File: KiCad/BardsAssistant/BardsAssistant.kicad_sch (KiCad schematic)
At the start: 70 parts, among them IC1 ESP32-S3-MINI-1-N8, J1 USB_C_Receptacle_USB2.0_16P, J2 Conn_01x24, J3 JST-PH-2-SMT-RA, Q1 Si1308EDL, Q3 AO3401A, SW1 SW_Push, SW2 SW_Push, SW3 SW_Push, SW4 SW_Push, SW5 SW_Push, SW6 SW_Push, U1 TPS63001, U2 USBLC6-2SC6, U3 MCP73831/2

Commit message: Added new KiCad revision
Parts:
- added R17, R4: 1R, Resistor_SMD:R_0603_1608Metric, symbol Device:R_Small_US
- added TP7, TP8, TP9: TestPoint, TestPoint:TestPoint_Pad_2.0x2.0mm, symbol Connector:TestPoint
- C1, C5, C6: LCSC (none) -> C19702; MPN (none) -> CL10A106KP8NNNC; Manufacturer (none) -> Samsung; Notes (none) -> X5R 10V; Status (none) -> Locked
- C10, C9: LCSC (none) -> C1779; MPN (none) -> CL21A475KAQNNNE; Manufacturer (none) -> Samsung; Status (none) -> Locked
- C11, C12, C15, C16, C17, C18, C19, C20: LCSC (none) -> C15849; MPN (none) -> CL10A105KA8NNNC; Manufacturer (none) -> Samsung; Status (none) -> Locked
- C13, C7, C8: LCSC (none) -> C15849; MPN (none) -> CL10A105KB8NNNC; Manufacturer (none) -> Samsung; Status (none) -> Locked
- C2: LCSC (none) -> C14663; MPN (none) -> CC0603KRX7R9BB104; Manufacturer (none) -> YAGEO; Notes (none) -> X5R 50V bc 10V is extended parts catalog in jlc.; Status (none) -> Locked
- C21, C22: LCSC (none) -> C19702; MPN (none) -> CL10A106KP8NNNC; Manufacturer (none) -> Samsung; Status (none) -> Locked
- C3: LCSC (none) -> C45783; MPN (none) -> CL21A226MAQNNNE; Manufacturer (none) -> Samsung; Notes (none) -> 25V; Status (none) -> Locked
- C4: footprint Capacitor_SMD:C_0805_2012Metric -> Capacitor_SMD:C_0603_1608Metric; LCSC (none) -> C14663; MPN (none) -> CC0603KRX7R9BB104; Manufacturer (none) -> Yaego; Notes (none) -> Using 50V bc 10v is extended parts catalog for jlc; Status (none) -> Locked
- D1: LCSC (none) -> C965844; MPN (none) -> XL-3227RGB-RF; Manufacturer (none) -> XINGLIGHT; Status (none) -> Locked
- D2: LCSC (none) -> C2480; MPN (none) -> SS14; Manufacturer (none) -> MDD(Microdiode Semiconductor); Status (none) -> Locked
- D3, D4: LCSC (none) -> C96512; MPN (none) -> ESD9B3.3ST5G; Manufacturer (none) -> onsemi; Status (none) -> Locked
- D5: LCSC (none) -> C2286; MPN (none) -> KT-0603R; Manufacturer (none) -> Hubei KENTO Elec; Status (none) -> Locked
- D6, D7, D8: LCSC (none) -> C77336; MPN (none) -> MBR0530; Manufacturer (none) -> Jiangsu Changjing Electronics Technology Co., Ltd.; Status (none) -> Locked
- D9: footprint LED_SMD:LED_0603_1608Metric -> LED_SMD:LED_0805_2012Metric; LCSC (none) -> C2297; MPN (none) -> KT-0805G; Manufacturer (none) -> Hubei KENTO Elec; Status (none) -> Locked
- F1: footprint Fuse:Fuse_1206_3216Metric -> Fuse:Fuse_0805_2012Metric; LCSC (none) -> C5307781; MPN (none) -> JK-SMD0805-100-6; Manufacturer (none) -> Jinrui Electronic Materials Co.; Status (none) -> Locked
- FB1: LCSC (none) -> C85840; MPN (none) -> BLM21PG221SN1D; Manufacturer (none) -> Murata Electronics; Status (none) -> Locked
- IC1: footprint ESP32S3MINI1N8 -> ESP32-S3-MINI-1-N8:ESP32S3MINI1N8; Height 2.55 -> (none); LCSC (none) -> C2913206; MPN (none) -> ESP32-S3-MINI-1-N8; Manufacturer (none) -> Espressif Systems; Mouser Part Number 356-ESP32-S3-MINI1N8 -> (none); Mouser Price/Stock https://www.mouser.co.uk/ProductDetail/Espressif-Systems/ES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 -> (none); Status (none) -> Locked
- J1: LCSC (none) -> C5143397; MPN (none) -> USB4110-GF-A; Manufacturer (none) -> GCT; Status (none) -> Locked
- J2: footprint Connector_FFC-FPC:Hirose_FH12-24S-0.5SH_1x24-1MP_P0.50mm_Horizontal -> BardAssLibrary:FPC-SMD_KH-FG0.5-H2.0-24PIN; LCSC (none) -> C2797213; MPN (none) -> KH-FG0.5-H2.0-24PIN; Manufacturer (none) -> Shenzhen Kinghelm Elec; Notes (none) -> Verify against data sheet
- J3: LCSC (none) -> C157932; MPN (none) -> S2B-PH-K-S-GW; Manufacturer (none) -> JST; Status (none) -> Locked
- L1: LCSC (none) -> C53663; MPN (none) -> SWPA6045S680MT; Manufacturer (none) -> Sunlord; Status (none) -> Locked
- L2: footprint Inductor_SMD:L_Wuerth_MAPI-4020 -> BardAssLibrary:SMNR5040_2R2MT_BA; LCSC (none) -> C9941; MPN (none) -> SMNR5040-2R2MT; Manufacturer (none) -> Shenzhen Shun Xiang Nuo Electronics; Status (none) -> Locked
- Q1: LCSC (none) -> C469327; MPN (none) -> SI1308EDL-T1-GE3; Manufacturer (none) -> Vishay; Status (none) -> Locked
- Q3: LCSC (none) -> C15127; MPN (none) -> AO3401A; Manufacturer (none) -> Alpha & Omega Semicon; Status (none) -> Locked
- R1, R10, R2: LCSC (none) -> C25905; MPN (none) -> 0402WGF5101TCE; Manufacturer (none) -> Uni-Royal; Status (none) -> Locked
- R11, R14, R16: LCSC (none) -> C23138; MPN (none) -> 0603WAF3300T5E; Manufacturer (none) -> Uni-Royal; Status (none) -> Locked
- R12, R13: LCSC (none) -> C25117; MPN (none) -> 0402WGF4700TCE; Manufacturer (none) -> Uni-Royal; Status (none) -> Locked
- R15: LCSC (none) -> C25076; MPN (none) -> 0402WGF1000TCE; Manufacturer (none) -> Uni-Royal; Status (none) -> Locked
- R3, R5, R7, R8: LCSC (none) -> C25744; MPN (none) -> 0402WGF1002TCE; Manufacturer (none) -> Uni-Royal; Status (none) -> Locked
- R6: LCSC (none) -> C25741; MPN (none) -> 0402WGF1003TCE; Manufacturer (none) -> Uni-Royal; Status (none) -> Locked
- R9: value 3R -> 1R; footprint Resistor_SMD:R_0402_1005Metric -> Resistor_SMD:R_0603_1608Metric; LCSC (none) -> C22936; MPN (none) -> 0603WAF100KT5E; Manufacturer (none) -> Uni-Royal; Status (none) -> Locked
- SW1, SW2, SW3, SW4, SW5, SW6: footprint Button_Switch_SMD:SW_Push_1P1T_XKB_TS-1187A -> Button_Switch_SMD:SW_SPST_TS-1088-xR020; LCSC (none) -> C720477; MPN (none) -> TS-1088-AR02016; Manufacturer (none) -> XUNPU; Status (none) -> Locked
- U1: LCSC (none) -> C28060; MPN (none) -> TPS63001DRCR; Manufacturer (none) -> Texas Instruments; Notes (none) -> Check footprint; Status (none) -> Locked
- U2: LCSC (none) -> C7519; MPN (none) -> USBLC6-2SC6; Manufacturer (none) -> STMicroelectronics; Status (none) -> Locked
- U3: LCSC (none) -> C424093; MPN (none) -> MCP73831T-2ACI/OT; Manufacturer (none) -> Microchip Tech; Notes (none) -> Exact Adafuit chip used; Status (none) -> Locked
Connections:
- net GND: now also R17.2; no longer R9.2
- net at IC1.25 (IO21): now also TP7.1
- net TP8: now reaches IC1.5 (IO1)
- net TP8: now also TP8.1
- net TP9: now reaches IC1.6 (IO2)
- net TP9: now also TP9.1
- new net: R4.1, R9.2
- new net: R17.1, R4.2
- no-connect marks 39 -> 36
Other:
- note added: "R4,R9,R17 Originally 3R, but extended parts so 1R x 3 in series should be close enough"
- note removed: "HRO TYPE-C-31-M-12"
- moved on the sheet: R9

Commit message: updated pcb v1
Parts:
- removed TP6: TestPoint, TestPoint:TestPoint_Pad_2.0x2.0mm, symbol Connector:TestPoint
- C1, C21, C22, C5, C6: LCSC C19702 -> (none); LCSC Part # (none) -> C19702
- C10, C9: LCSC C1779 -> (none); LCSC Part # (none) -> C1779
- C11, C12, C15, C16, C17, C18, C19, C20: LCSC C15849 -> (none); LCSC Part # (none) -> C1712; MPN CL10A105KA8NNNC -> CL21B105KAFNFNE
- C13, C7, C8: LCSC C15849 -> (none); LCSC Part # (none) -> C1712; MPN CL10A105KB8NNNC -> CL21B105KAFNFNE
- C2: LCSC C14663 -> (none); LCSC Part # (none) -> C14663; Notes X5R 50V bc 10V is extended parts catalog in jlc. -> (none)
- C3: LCSC C45783 -> (none); LCSC Part # (none) -> C45783
- C4: LCSC C14663 -> (none); LCSC Part # (none) -> C14663; Notes Using 50V bc 10v is extended parts catalog for jlc -> (none)
- D1: LCSC C965844 -> (none); LCSC Part # (none) -> C965844
- D2: LCSC C2480 -> (none); LCSC Part # (none) -> C2480
- D3, D4: LCSC C96512 -> (none); LCSC Part # (none) -> C96512
- D5: LCSC C2286 -> (none); LCSC Part # (none) -> C2286
- D6, D7, D8: LCSC C77336 -> (none); LCSC Part # (none) -> C77336
- D9: LCSC C2297 -> (none); LCSC Part # (none) -> C2297
- F1: LCSC C5307781 -> (none); LCSC Part # (none) -> C5307781
- FB1: LCSC C85840 -> (none); LCSC Part # (none) -> C85840
- IC1: LCSC C2913206 -> (none); LCSC Part # (none) -> C2913206
- J1: LCSC C5143397 -> (none); LCSC Part # (none) -> C5143397
- J2: LCSC C2797213 -> (none); LCSC Part # (none) -> C2797213; Notes Verify against data sheet -> (none); Status (none) -> Locked
- J3: LCSC C157932 -> (none); LCSC Part # (none) -> C157932
- L1: LCSC C53663 -> (none); LCSC Part # (none) -> C53663
- L2: LCSC C9941 -> (none); LCSC Part # (none) -> C9941
- Q1: LCSC C469327 -> (none); LCSC Part # (none) -> C469327
- Q3: LCSC C15127 -> (none); LCSC Part # (none) -> C15127
- R1, R10, R2: LCSC C25905 -> (none); LCSC Part # (none) -> C25905
- R11, R14, R16: LCSC C23138 -> (none); LCSC Part # (none) -> C23138
- R12, R13: LCSC C25117 -> (none); LCSC Part # (none) -> C25117
- R15: LCSC C25076 -> (none); LCSC Part # (none) -> C25076
- R17, R4, R9: LCSC C22936 -> (none); LCSC Part # (none) -> C22936
- R3, R5, R7, R8: LCSC C25744 -> (none); LCSC Part # (none) -> C25744
- R6: LCSC C25741 -> (none); LCSC Part # (none) -> C25741
- SW1, SW2, SW3, SW4, SW5, SW6: LCSC C720477 -> (none); LCSC Part # (none) -> C720477
- TP1: Notes TP1 Expected 5V -> (none); Status (none) -> Locked; now left out of the parts list
- TP2: Notes Empty ~3.2v, nominal ~3.7, full ~4.2 -> (none); Status (none) -> Locked; now left out of the parts list
- TP3: Notes plugged SYS ≈ 4.7-5V, unplugged SYS ≈ BAT -> (none); Status (none) -> Locked; now left out of the parts list
- TP4, TP7, TP8, TP9: Status (none) -> Locked; now left out of the parts list
- TP5: value TestPoint -> GND; Notes Ground -> (none); Status (none) -> Locked; now left out of the parts list
- U1: LCSC C28060 -> (none); LCSC Part # (none) -> C28060; Notes Check footprint -> (none)
- U2: LCSC C7519 -> (none); LCSC Part # (none) -> C7519
- U3: LCSC C424093 -> (none); LCSC Part # (none) -> C424093
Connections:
- net +3.3V is gone; now on net +3V3: D1.4 (A)
- net VDD33 is gone; now on net +3V3: C10.2, L1.1
- net at IC1.33 (IO37): now also TP8.1
- net at IC1.34 (IO38): now also TP9.1
- net TP8: no longer names the net of IC1.5 (IO1)
- net TP8: no longer TP8.1
- net TP9: no longer names the net of IC1.6 (IO2)
- net TP9: no longer TP9.1
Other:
- note removed: "MINI-1 Data sheet"
- moved on the sheet: TP7

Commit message: Update KiCad schematic, PCB, and library files
- Update schematic and PCB layout
- Add LED-SMD-SM1210RGB footprint to BardAssLibrary
- Remove old Gerber exports and production files, update with new
- Remove BAV1.zip
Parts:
- removed D1: XL-3227RGB-RF, BardAssLibrary:LED_XL-3227RGB-RF, symbol Device:LED_RGBA
- added D1: SM1210RGB, BardAssLibrary:LED_XL-3227RGB-RF, symbol BARDSASS:LED_RGBA_SM1210RGB_BIVAR
- added R18, R19: 22R, Resistor_SMD:R_0805_2012Metric, symbol Device:R_Small_US
- C1, C5, C6: footprint Capacitor_SMD:C_0603_1608Metric -> Capacitor_SMD:C_0805_2012Metric; LCSC Part # C19702 -> (none); MPN CL10A106KP8NNNC -> CL21B106KOYNNWE; Mouser Part Number (none) -> 187-CL21B106KOYNNWE; Notes X5R 10V -> (none)
- C10, C9: LCSC Part # C1779 -> (none); MPN CL21A475KAQNNNE -> CC0805KKX7R8BB475; Manufacturer Samsung -> Yageo; Mouser Part Number (none) -> 603-CC805KKX7R8BB475
- C11, C12, C15, C16, C17, C18, C19, C20: LCSC Part # C1712 -> (none); MPN CL21B105KAFNFNE -> CC0805KFX7R8BB105; Manufacturer Samsung -> Yageo; Mouser Part Number (none) -> 603-CC805KFX7R8BB105
- C13, C7, C8: footprint Capacitor_SMD:C_0603_1608Metric -> Capacitor_SMD:C_0805_2012Metric; LCSC Part # C1712 -> (none); MPN CL21B105KAFNFNE -> CC0805KFX7R8BB105; Manufacturer Samsung -> Yageo; Mouser Part Number (none) -> 603-CC805KFX7R8BB105
- C2: footprint Capacitor_SMD:C_0603_1608Metric -> Capacitor_SMD:C_0805_2012Metric; LCSC Part # C14663 -> (none); MPN CC0603KRX7R9BB104 -> CC0805KRX7R8BB104; Manufacturer YAGEO -> Yageo; Mouser Part Number (none) -> 603-CC805KRX7R8BB104
- C21, C22: LCSC Part # C19702 -> (none); MPN CL10A106KP8NNNC -> CL21B106KOYNNWE; Mouser Part Number (none) -> 187-CL21B106KOYNNWE
- C3: LCSC Part # C45783 -> (none); MPN CL21A226MAQNNNE -> CC0805MFX5R8BB226; Manufacturer Samsung -> Yageo; Mouser Part Number (none) -> 603-CC0805MFX5R8BB22
- C4: footprint Capacitor_SMD:C_0603_1608Metric -> Capacitor_SMD:C_0805_2012Metric; LCSC Part # C14663 -> (none); MPN CC0603KRX7R9BB104 -> CC0805KRX7R8BB104; Manufacturer Yaego -> Yageo; Mouser Part Number (none) -> 603-CC805KRX7R8BB104
- D3, D4: LCSC Part # C96512 -> (none); Mouser Part Number (none) -> 863-ESD9B3.3ST5G
- D5: footprint LED_SMD:LED_0603_1608Metric -> LED_SMD:LED_0805_2012Metric; MPN KT-0603R -> 150080SS75000; Manufacturer Hubei KENTO Elec -> Wurth Elektronik; Mouser Part Number (none) -> 710-150080SS75000
- IC1: Mouser Part Number (none) -> 356-ESP32-S3-MINI1N8
- R1, R2: footprint Resistor_SMD:R_0402_1005Metric -> Resistor_SMD:R_0805_2012Metric; LCSC Part # C25905 -> C27834; MPN 0402WGF5101TCE -> 0805W8F5101T5E
- R10: value 5K -> 5K1; footprint Resistor_SMD:R_0402_1005Metric -> Resistor_SMD:R_0805_2012Metric; LCSC Part # C25905 -> C27834; MPN 0402WGF5101TCE -> 0805W8F5101T5E
- R11, R14, R16: footprint Resistor_SMD:R_0402_1005Metric -> Resistor_SMD:R_0805_2012Metric; LCSC Part # C23138 -> C17630; MPN 0603WAF3300T5E -> 0805W8F3300T5E
- R12, R13: footprint Resistor_SMD:R_0402_1005Metric -> Resistor_SMD:R_0805_2012Metric; LCSC Part # C25117 -> C17710; MPN 0402WGF4700TCE -> 0805W8F4700T5E
- R15: footprint Resistor_SMD:R_0402_1005Metric -> Resistor_SMD:R_0805_2012Metric; LCSC Part # C25076 -> C17408; MPN 0402WGF1000TCE -> 0805W8F1000T5E
- R17, R4, R9: footprint Resistor_SMD:R_0603_1608Metric -> Resistor_SMD:R_0805_2012Metric; LCSC Part # C22936 -> C25271; MPN 0603WAF100KT5E -> 0805W8F100KT5E
- R3, R5, R7, R8: footprint Resistor_SMD:R_0402_1005Metric -> Resistor_SMD:R_0805_2012Metric; LCSC Part # C25744 -> C17414; MPN 0402WGF1002TCE -> 0805W8F1002T5E
- R6: footprint Resistor_SMD:R_0402_1005Metric -> Resistor_SMD:R_0805_2012Metric; LCSC Part # C25741 -> C149504; MPN 0402WGF1003TCE -> 0805W8F1003T5E
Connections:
- net +3V3: now also D1.1 (A)
- net D+: now also R19.1; no longer J1.A6 (D+), J1.B6 (D+)
- net D-: now also R18.1; no longer J1.A7 (D-), J1.B7 (D-)
- net at IC1.21 (IO17): now also R14.2; no longer R11.2
- net at IC1.22 (IO18): now also R11.2; no longer R14.2
- net at R16.1: now also D1.4 (BK)
- net at R14.1: now also D1.3 (GK)
- net at R11.1: now also D1.2 (RK)
- new net: J1.A6 (D+), J1.B6 (D+), R19.2
- new net: J1.A7 (D-), J1.B7 (D-), R18.2
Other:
- note added: "0805 Components and smaller board size than V1.0. Same board size as 1.1, but mouser part numbers instead. 1.1 has smaller part sizes for jlcpcb assembly."
- title: Bards Assistant V1 -> Bards Assistant V1.2

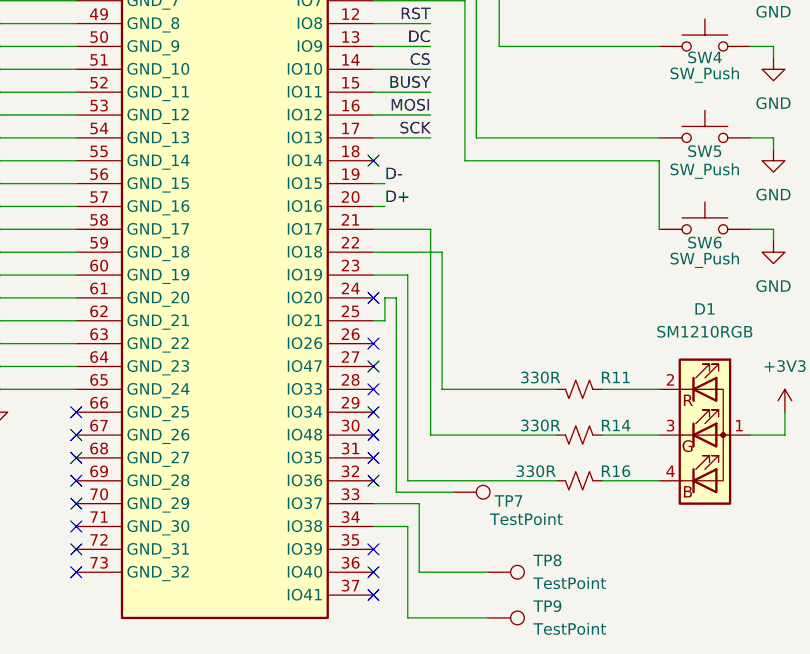
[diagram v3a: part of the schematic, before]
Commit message: update d-, d+ connection
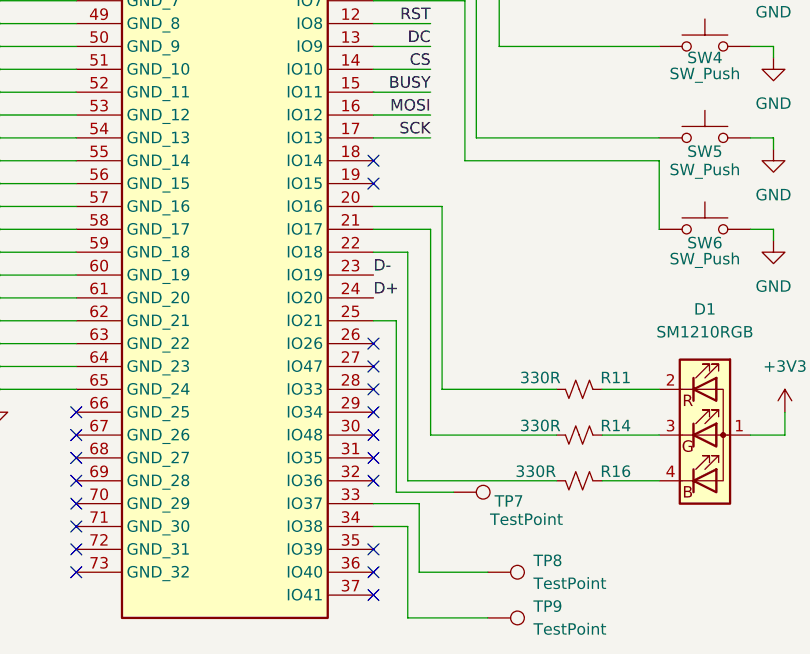
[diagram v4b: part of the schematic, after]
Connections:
- net D+: now also IC1.24 (IO20); no longer IC1.20 (IO16)
- net D-: now also IC1.23 (IO19); no longer IC1.19 (IO15)
- net at R11.2: now also IC1.20 (IO16); no longer IC1.22 (IO18)
- net at R16.2: now also IC1.22 (IO18); no longer IC1.23 (IO19)
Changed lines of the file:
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@@
 	)
 	(no_connect
+		(at 184.15 114.3)
+	)
+	(no_connect
 		(at 90.17 140.97)
 	)
@@
 	)
 	(no_connect
-		(at 184.15 127)
-	)
-	(no_connect
 		(at 90.17 143.51)
 	)
@@
 	(wire
 		(pts
-			(xy 185.42 129.54) (xy 184.15 129.54)
+			(xy 184.15 129.54) (xy 186.69 129.54)
 		)
 		(stroke
@@
 	(wire
 		(pts
-			(xy 31.75 172.72) (xy 31.75 175.26)
+			(xy 186.69 148.59) (xy 186.69 129.54)
 		)
 		(stroke
@@
 	(wire
 		(pts
-			(xy 135.89 38.1) (xy 135.89 34.29)
+			(xy 31.75 172.72) (xy 31.75 175.26)
 		)
 		(stroke
@@
 	(wire
 		(pts
-			(xy 142.24 78.74) (xy 142.24 81.28)
+			(xy 135.89 38.1) (xy 135.89 34.29)
 		)
 		(stroke
@@
 	(wire
 		(pts
-			(xy 45.72 104.14) (xy 45.72 105.41)
+			(xy 142.24 78.74) (xy 142.24 81.28)
 		)
 		(stroke
@@
 	(wire
 		(pts
-			(xy 214.63 69.85) (xy 214.63 76.2)
+			(xy 45.72 104.14) (xy 45.72 105.41)
 		)
 		(stroke
@@
 	(wire
 		(pts
-			(xy 124.46 39.37) (xy 124.46 38.1)
+			(xy 214.63 69.85) (xy 214.63 76.2)
 		)
 		(stroke
@@
 	(wire
 		(pts
-			(xy 66.04 173.99) (xy 66.04 176.53)
+			(xy 124.46 39.37) (xy 124.46 38.1)
 		)
 		(stroke
@@
 	(wire
 		(pts
-			(xy 186.69 127) (xy 186.69 148.59)
+			(xy 66.04 173.99) (xy 66.04 176.53)
 		)
 		(stroke
@@
 	(wire
 		(pts
-			(xy 187.96 147.32) (xy 187.96 124.46)
+			(xy 187.96 121.92) (xy 187.96 147.32)
 		)
 		(stroke
@@
 	(wire
 		(pts
-			(xy 184.15 121.92) (xy 191.77 121.92)
-		)
-		(stroke
-			(width 0)
-			(type default)
-		)
-	)
-	(wire
-		(pts
 			(xy 81.28 166.37) (xy 81.28 163.83)
 		)
@@
 	(wire
 		(pts
-			(xy 185.42 114.3) (xy 184.15 114.3)
-		)
-		(stroke
-			(width 0)
-			(type default)
-		)
-	)
-	(wire
-		(pts
 			(xy 73.66 69.85) (xy 73.66 72.39)
 		)
@@
 	(wire
 		(pts
-			(xy 187.96 124.46) (xy 184.15 124.46)
-		)
-		(stroke
-			(width 0)
-			(type default)
-		)
-	)
-	(wire
-		(pts
 			(xy 142.24 88.9) (xy 142.24 91.44)
 		)
@@
 	(wire
 		(pts
-			(xy 185.42 116.84) (xy 184.15 116.84)
+			(xy 184.15 116.84) (xy 191.77 116.84)
 		)
 		(stroke
@@
 	(wire
 		(pts
-			(xy 185.42 127) (xy 185.42 129.54)
-		)
-		(stroke
-			(width 0)
-			(type default)
-		)
-	)
-	(wire
-		(pts
 			(xy 45.72 153.67) (xy 45.72 166.37)
 		)
@@
 	(wire
 		(pts
-			(xy 185.42 127) (xy 186.69 127)
-		)
-		(stroke
-			(width 0)
-			(type default)
-		)
-	)
-	(wire
-		(pts
 			(xy 62.23 82.55) (xy 62.23 83.82)
 		)
@@
 	(wire
 		(pts
-			(xy 191.77 121.92) (xy 191.77 137.16)
+			(xy 191.77 116.84) (xy 191.77 137.16)
 		)
 		(stroke
@@
 		)
 	)
+	(wire
+		(pts
+			(xy 187.96 121.92) (xy 184.15 121.92)
+		)
+		(stroke
+			(width 0)
+			(type default)
+		)
+	)
 	(label "CS"
 		(at 77.47 156.21 0)
@@
 	)
 	(label "D-"
-		(at 185.42 114.3 0)
+		(at 184.15 124.46 0)
 		(effects
 			(font
@@
 	)
 	(label "D+"
-		(at 185.42 116.84 0)
+		(at 184.15 127 0)
 		(effects
 			(font
